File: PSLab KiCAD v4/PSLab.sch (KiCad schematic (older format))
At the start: 69 parts, among them CON1 USB-MICRO-B, J1 Programmer, J12 Sensors, J2 SQRs, J3 LA, J4 OSC_Pins, J6 I2C, J7 IDs, J8 TX_RX_ES, J9 Test_Vs, P7 NRF, Q2 MMBT3904, Q3 MMBT3906, U1 MCP2200, U15 ESP8266, U2 74HC126, U3 PIC24EP256GP204, U4 TC1240A, U5 7660, U6 LM1117-3.3, X1 12MHz

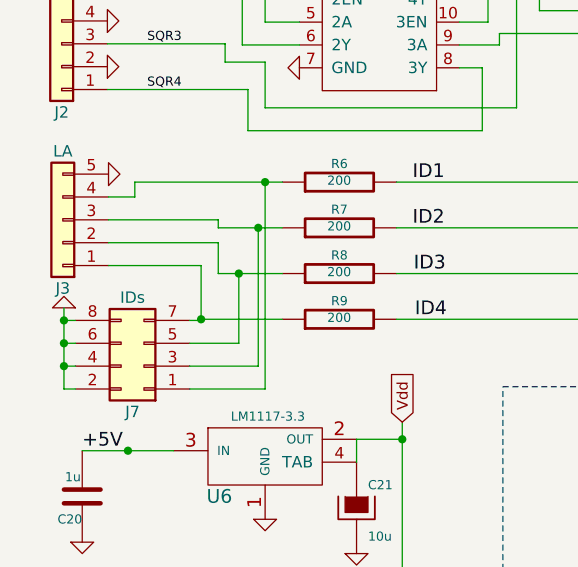
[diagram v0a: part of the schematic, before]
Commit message: Optimizing layout
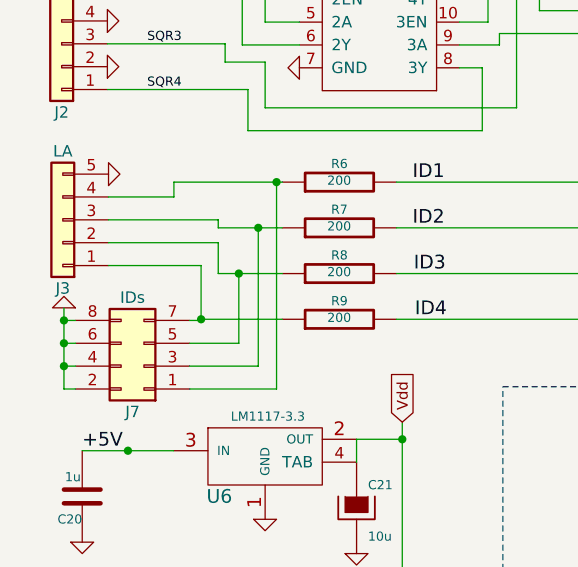
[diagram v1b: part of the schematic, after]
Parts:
- C1, C10, C13, C17, C2, C4, C5, C8, C9: footprint Capacitors_SMD:C_0201 -> Capacitors_SMD:C_0603
- C15, C20, C21: footprint Capacitors_SMD:C_0402 -> Capacitors_SMD:C_0603
- R1, R10, R11, R12, R13, R2, R3, R4, R49, R5, R52, R53, R54, R55, R56, R57, R6, R7, R8, R9: footprint Resistors_SMD:R_0201 -> Resistors_SMD:R_0603

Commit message: Programmer pin header adjustments
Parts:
- P7: footprint Custom_Components:nRF24L01_Breakout_2 -> Pin_Headers:Pin_Header_Straight_2x04_Pitch2.54mm
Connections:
- net GND: now also J1.4 (Pin_4); no longer J1.2 (Pin_2)
- net MCLR: now also J1.2 (Pin_2); no longer J1.6 (Pin_6)
- net PGC2: now also J1.6 (Pin_6); no longer J1.5 (Pin_5)
- net PGD2: now also J1.5 (Pin_5); no longer J1.4 (Pin_4)
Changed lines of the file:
@@
 F 0 "P7" H 1505 7675 50  0000 C CNN
 F 1 "NRF" H 1505 7175 50  0000 C CNN
-F 2 "Custom_Components:nRF24L01_Breakout_2" H 1505 6225 60  0001 C CNN
+F 2 "Pin_Headers:Pin_Header_Straight_2x04_Pitch2.54mm" H 1505 6225 60  0001 C CNN
 F 3 "" H 1505 6225 60  0000 C CNN
 	1    1505 7425
@@
 Text GLabel 5020 1020 2    40   Input ~ 0
 PGD2
-Text GLabel 4670 7005 0    40   Input ~ 0
+Text GLabel 4670 7105 0    40   Input ~ 0
 PGD2
-Text GLabel 4670 7105 0    40   Input ~ 0
+Text GLabel 4670 7205 0    40   Input ~ 0
 PGC2
 $Comp
@@
 L GND-RESCUE-proto1 #PWR048
 U 1 1 5A56D115
-P 4670 6805
-F 0 "#PWR048" H 4670 6805 30  0001 C CNN
-F 1 "GND" H 4670 6735 30  0001 C CNN
-F 2 "" H 4670 6805 60  0000 C CNN
-F 3 "" H 4670 6805 60  0000 C CNN
-	1    4670 6805
-	0    1    1    0
-$EndComp
-Text GLabel 4670 7205 0    40   Input ~ 0
+P 4670 7005
+F 0 "#PWR048" H 4670 7005 30  0001 C CNN
+F 1 "GND" H 4670 6935 30  0001 C CNN
+F 2 "" H 4670 7005 60  0000 C CNN
+F 3 "" H 4670 7005 60  0000 C CNN
+	1    4670 7005
+	0    1    1    0
+$EndComp
+Text GLabel 4670 6805 0    40   Input ~ 0
 MCLR
 Text GLabel 4545 815  0    40   Input ~ 0

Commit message: Added Gerber files
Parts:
- added TP3, TP4: TEST, Measurement_Points:Measurement_Point_Round-SMD-Pad_Small, symbol TEST
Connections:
- net +5V: now also TP3.1
- net GND: now also TP4.1
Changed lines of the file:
@@
 	1550 5355 1550 4450
 Connection ~ 1550 4450
+$Comp
+L TEST TP3
+U 1 1 5A66A817
+P 850 1930
+F 0 "TP3" H 850 2230 50  0000 C BNN
+F 1 "TEST" H 850 2180 50  0000 C CNN
+F 2 "Measurement_Points:Measurement_Point_Round-SMD-Pad_Small" H 850 1930 50  0001 C CNN
+F 3 "" H 850 1930 50  0001 C CNN
+	1    850  1930
+	1    0    0    -1
+$EndComp
+$Comp
+L TEST TP4
+U 1 1 5A66B7F8
+P 2285 1925
+F 0 "TP4" H 2285 2225 50  0000 C BNN
+F 1 "TEST" H 2285 2175 50  0000 C CNN
+F 2 "Measurement_Points:Measurement_Point_Round-SMD-Pad_Small" H 2285 1925 50  0001 C CNN
+F 3 "" H 2285 1925 50  0001 C CNN
+	1    2285 1925
+	1    0    0    -1
+$EndComp
+$Comp
+L GND-RESCUE-proto1 #PWR056
+U 1 1 5A66B8E0
+P 2285 1925
+F 0 "#PWR056" H 2285 1925 30  0001 C CNN
+F 1 "GND" H 2285 1855 30  0001 C CNN
+F 2 "" H 2285 1925 60  0000 C CNN
+F 3 "" H 2285 1925 60  0000 C CNN
+	1    2285 1925
+	1    0    0    -1
+$EndComp
 $EndSCHEMATC

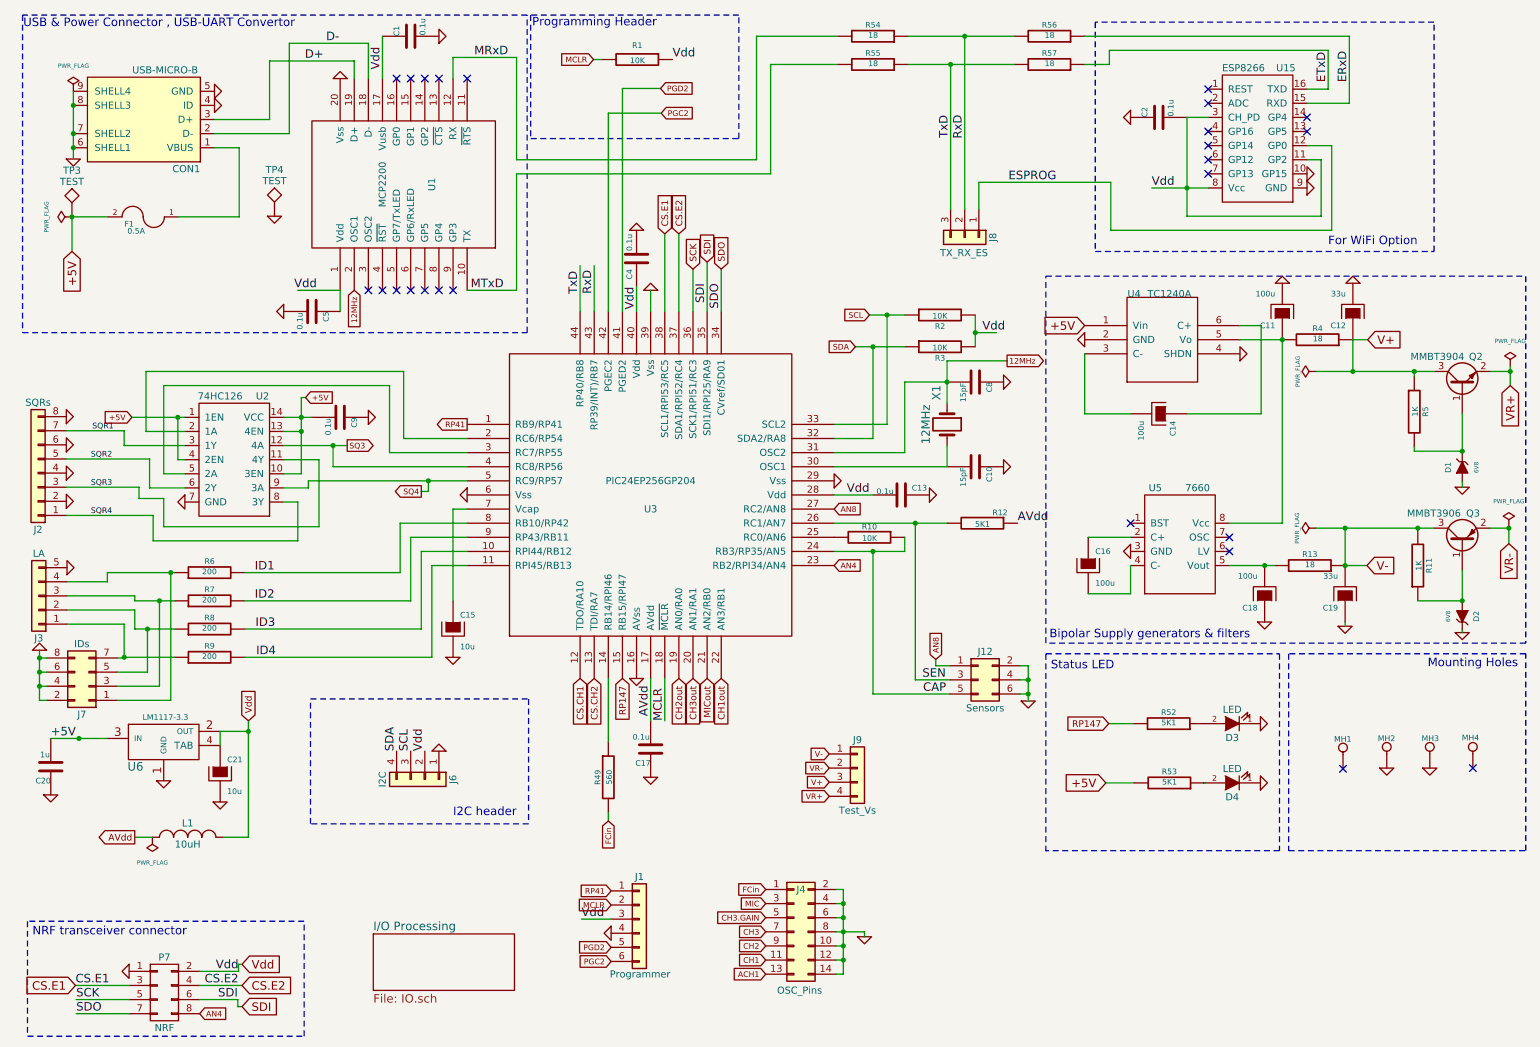
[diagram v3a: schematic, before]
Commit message: Added breakouts for MCP2200 & PIC24 (#36)
* Added breakouts for MCP2200

* Added guard rings for OSC

* Grounded mount holes

* Gerber files updated
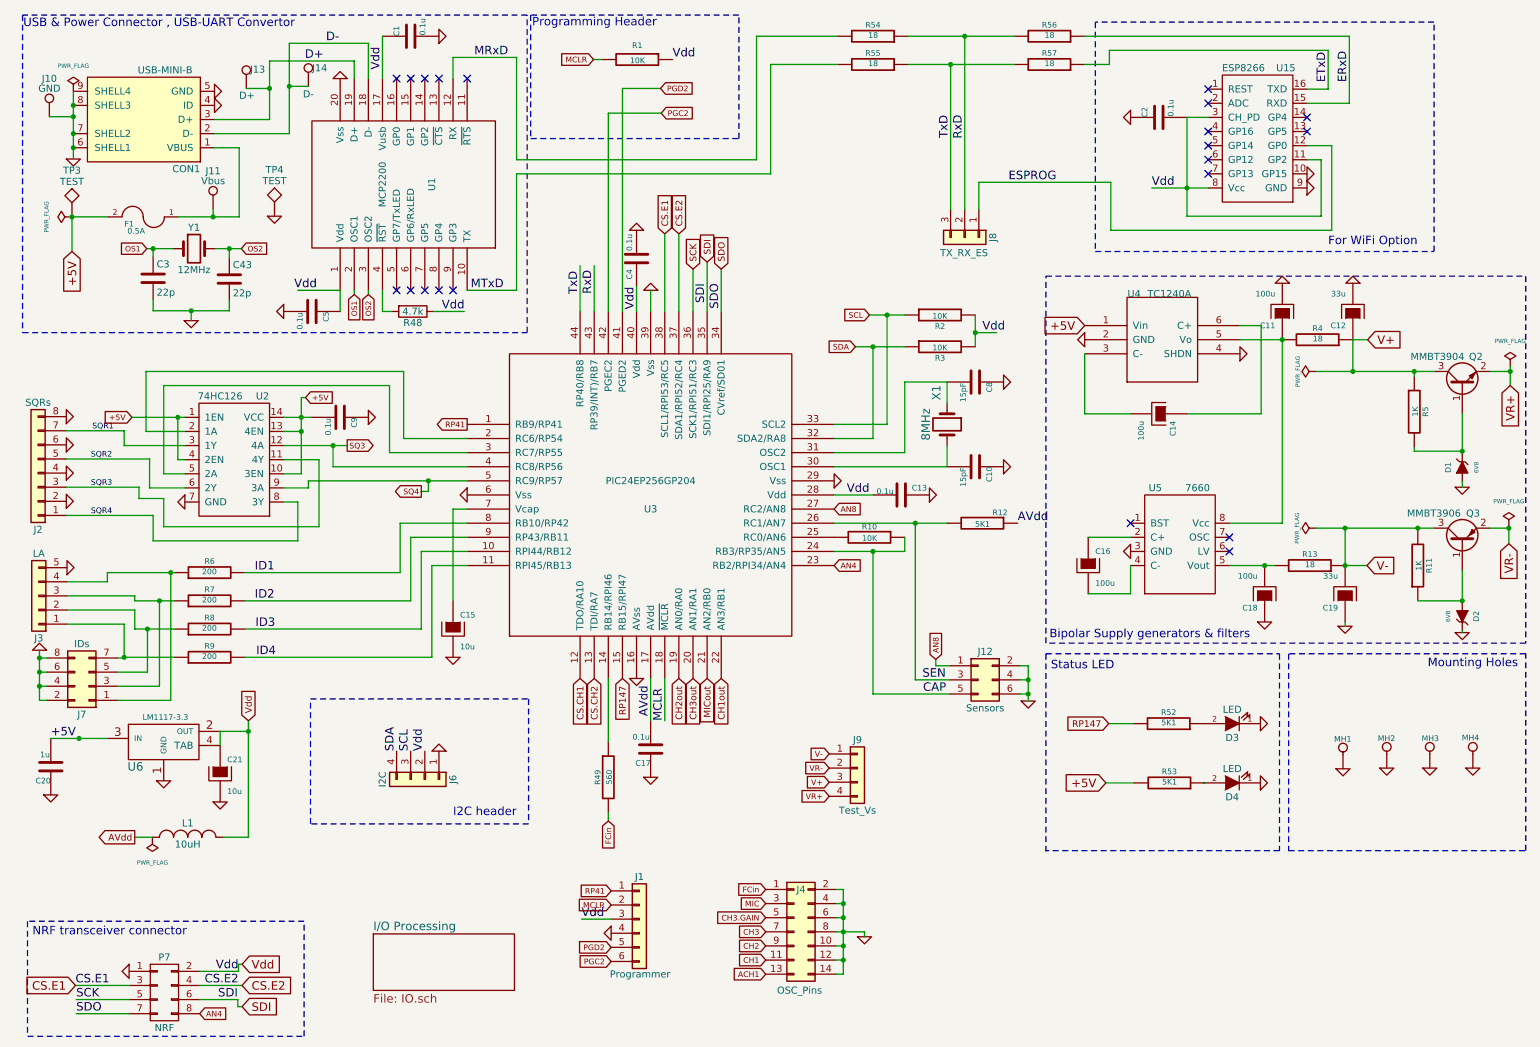
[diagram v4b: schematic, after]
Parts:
- added C3, C43: 22p, Capacitors_SMD:C_0603, symbol C
- added J10: GND, Measurement_Points:Measurement_Point_Square-SMD-Pad_Small, symbol TEST_1P
- added J11: Vbus, Measurement_Points:Measurement_Point_Square-SMD-Pad_Small, symbol TEST_1P
- added J13: D+, Measurement_Points:Measurement_Point_Square-SMD-Pad_Small, symbol TEST_1P
- added J14: D-, Measurement_Points:Measurement_Point_Square-SMD-Pad_Small, symbol TEST_1P
- added R48: 4.7k, Resistors_SMD:R_0603, symbol R
- added Y1: 12MHz, Crystals:Crystal_SMD_5032-2pin_5.0x3.2mm, symbol Crystal
- CON1: value USB-MICRO-B -> USB-MINI-B
- D3, D4: footprint LEDs:LED_0805 -> LEDs:LED_0603
- L1: footprint Inductors_SMD:L_0805 -> Inductors_SMD:L_0603
- X1: value 12MHz -> 8MHz; footprint Crystals:Crystal_HC49-U_Vertical -> Crystals:Crystal_SMD_5032-2pin_5.0x3.2mm
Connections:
- net D+: now also J13.1
- net D-: now also J14.1
- net GND: now also MH1.1, MH4.1, C3.2, C43.2, J10.1
- net Vdd: now also R48.1
- net OS2: now reaches U1.3 (OSC2)
- net OS2: now also C43.1, Y1.2
- net at U1.4 (~RST): now also R48.2
- net at CON1.1 (VBUS), F1.1: now also J11.1
- net 12MHz: no longer names the net of C8.2, U3.31 (OSC2), X1.1
- net 12MHz: no longer U1.2 (OSC1)
- new net OS1: C3.1, U1.2 (OSC1), Y1.1
- no-connect marks 25 -> 21
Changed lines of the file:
@@
 NoConn ~ 3450 2450
 NoConn ~ 3350 2450
-NoConn ~ 3050 2450
 $Comp
 L CONN_1 MH1
@@
 P 7050 3400
 F 0 "X1" H 6825 3325 60  0000 C CNN
-F 1 "12MHz" H 7050 3250 60  0000 C CNN
-F 2 "Crystals:Crystal_HC49-U_Vertical" H 7050 3400 60  0001 C CNN
+F 1 "8MHz" H 7050 3250 60  0000 C CNN
+F 2 "Crystals:Crystal_SMD_5032-2pin_5.0x3.2mm" H 7050 3400 60  0001 C CNN
 F 3 "" H 7050 3400 60  0000 C CNN
 	1    7050 3400
@@
 F 0 "L1" H 1670 6425 50  0000 C CNN
 F 1 "10uH" H 1670 6275 50  0000 C CNN
-F 2 "Inductors_SMD:L_0805" H 1670 6325 60  0001 C CNN
+F 2 "Inductors_SMD:L_0603" H 1670 6325 60  0001 C CNN
 F 3 "" H 1670 6325 60  0000 C CNN
 	1    1670 6325
@@
 Text GLabel 3325 3875 0    40   Output ~ 0
 SQ4
-NoConn ~ 2950 2450
 $Comp
 L GND-RESCUE-proto1 #PWR041
@@
 Text GLabel 1755 7575 2    40   Input ~ 0
 AN4
-Text GLabel 7475 2950 2    40   Output ~ 0
-12MHz
-Text GLabel 2850 2450 3    40   Input ~ 0
-12MHz
 Text GLabel 2800 3550 2    40   Output ~ 0
 SQ3
@@
 F 0 "D3" H 9070 5620 50  0000 C CNN
 F 1 "LED" H 9070 5420 50  0000 C CNN
-F 2 "LEDs:LED_0805" H 9070 5520 60  0001 C CNN
+F 2 "LEDs:LED_0603" H 9070 5520 60  0001 C CNN
 F 3 "" H 9070 5520 60  0000 C CNN
 	1    9070 5520
@@
 F 0 "D4" H 9070 6040 50  0000 C CNN
 F 1 "LED" H 9070 5840 50  0000 C CNN
-F 2 "LEDs:LED_0805" H 9070 5940 60  0001 C CNN
+F 2 "LEDs:LED_0603" H 9070 5940 60  0001 C CNN
 F 3 "" H 9070 5940 60  0000 C CNN
 	1    9070 5940
@@
 $EndComp
 $Comp
-L USB-MINI-B CON1
-U 1 1 556D8B03
-P 1360 1240
-F 0 "CON1" H 1060 1590 50  0000 C CNN
-F 1 "USB-MICRO-B" H 1210 890 50  0000 C CNN
-F 2 "Connectors:USB_Micro-B" H 1360 1140 50  0001 C CNN
-F 3 "" H 1360 1140 50  0000 C CNN
-	1    1360 1240
-	-1   0    0    1
-$EndComp
-$Comp
 L Conn_01x03 J8
 U 1 1 5A320F8A
@@
 	0    -1   -1   0
 $EndComp
-NoConn ~ 9855 5840
-NoConn ~ 10775 5835
 $Comp
 L Conn_02x03_Odd_Even J12
@@
 	2030 7275 1755 7275
 Wire Wire Line
-	860  1040 860  1520
-Connection ~ 860  1440
-Wire Wire Line
 	1375 3450 1650 3450
 Wire Wire Line
@@
 Wire Wire Line
 	1420 6325 1295 6325
-Wire Wire Line
-	7050 2950 7050 3250
-Wire Wire Line
-	7050 2950 7475 2950
 Connection ~ 2700 3550
 Wire Wire Line
@@
 Wire Wire Line
 	7050 3700 7050 3550
-Connection ~ 7050 3100
 Wire Wire Line
 	2030 7225 2030 7275
@@
 	2390 1340 1860 1340
 Wire Wire Line
-	865  1340 860  1340
-Connection ~ 860  1340
+	860  1340 865  1340
 Wire Wire Line
 	865  1140 860  1140
-Connection ~ 860  1140
 Wire Wire Line
 	1605 1930 2035 1930
@@
 	1    0    0    -1
 $EndComp
+$Comp
+L USB-MINI-B CON1
+U 1 1 5A6CB48C
+P 1360 1240
+F 0 "CON1" H 1060 1590 50  0000 C CNN
+F 1 "USB-MINI-B" H 1210 890 50  0000 C CNN
+F 2 "Connectors:USB_Micro-B" H 1360 1140 50  0001 C CNN
+F 3 "" H 1360 1140 50  0000 C CNN
+	1    1360 1240
+	-1   0    0    1
+$EndComp
+Wire Wire Line
+	860  1040 860  1520
+Connection ~ 860  1440
+Connection ~ 860  1340
+Connection ~ 860  1140
+$Comp
+L R R48
+U 1 1 5A6CD97F
+P 3265 2600
+F 0 "R48" V 3345 2600 50  0000 C CNN
+F 1 "4.7k" V 3265 2600 50  0000 C CNN
+F 2 "Resistors_SMD:R_0603" V 3195 2600 50  0001 C CNN
+F 3 "" H 3265 2600 50  0001 C CNN
+	1    3265 2600
+	0    1    1    0
+$EndComp
+Wire Wire Line
+	3050 2450 3050 2600
+Wire Wire Line
+	3050 2600 3115 2600
+Text Label 3470 2600 0    60   ~ 0
+Vdd
+Wire Wire Line
+	3415 2600 3630 2600
+$Comp
+L Crystal Y1
+U 1 1 5A6D25F9
+P 1715 2155
+F 0 "Y1" H 1715 2305 50  0000 C CNN
+F 1 "12MHz" H 1715 2005 50  0000 C CNN
+F 2 "Crystals:Crystal_SMD_5032-2pin_5.0x3.2mm" H 1715 2155 50  0001 C CNN
+F 3 "" H 1715 2155 50  0001 C CNN
+	1    1715 2155
+	1    0    0    -1
+$EndComp
+$Comp
+L C C3
+U 1 1 5A6D2A55
+P 1425 2365
+F 0 "C3" H 1450 2465 50  0000 L CNN
+F 1 "22p" H 1450 2265 50  0000 L CNN
+F 2 "Capacitors_SMD:C_0603" H 1463 2215 50  0001 C CNN
+F 3 "" H 1425 2365 50  0001 C CNN
+	1    1425 2365
+	1    0    0    -1
+$EndComp
+$Comp
+L C C43
+U 1 1 5A6D2B78
+P 1965 2370
+F 0 "C43" H 1990 2470 50  0000 L CNN
+F 1 "22p" H 1990 2270 50  0000 L CNN
+F 2 "Capacitors_SMD:C_0603" H 2003 2220 50  0001 C CNN
+F 3 "" H 1965 2370 50  0001 C CNN
+	1    1965 2370
+	1    0    0    -1
+$EndComp
+Wire Wire Line
+	1865 2155 2050 2155
+Wire Wire Line
+	1965 2155 1965 2220
+$Comp
+L GND-RESCUE-proto1 #PWR057
+U 1 1 5A6D3C13
+P 1695 2665
+F 0 "#PWR057" H 1695 2665 30  0001 C CNN
+F 1 "GND" H 1695 2595 30  0001 C CNN
+F 2 "" H 1695 2665 60  0000 C CNN
+F 3 "" H 1695 2665 60  0000 C CNN
+	1    1695 2665
+	1    0    0    -1
+$EndComp
+Wire Wire Line
+	1380 2155 1565 2155
+Wire Wire Line
+	1425 2155 1425 2215
+Wire Wire Line
+	1425 2515 1425 2595
+Wire Wire Line
+	1425 2595 1965 2595
+Wire Wire Line
+	1965 2595 1965 2520
+Wire Wire Line
+	1695 2665 1695 2595
+Connection ~ 1695 2595
+Text GLabel 1380 2155 0    39   Input ~ 0
+OS1
+Text GLabel 2050 2155 2    39   Input ~ 0
+OS2
+Connection ~ 1965 2155
+Connection ~ 1425 2155
+Text GLabel 2850 2480 3    39   Input ~ 0
+OS1
+Wire Wire Line
+	2850 2480 2850 2450
+Text GLabel 2950 2480 3    39   Input ~ 0
+OS2
+Wire Wire Line
+	2950 2480 2950 2450
+Wire Wire Line
+	7050 3250 7050 3100
+$Comp
+L TEST_1P J13
+U 1 1 5A6F40E4
+P 2085 1020
+F 0 "J13" H 2165 1155 50  0000 C CNN
+F 1 "D+" H 2090 970 50  0000 C CNN
+F 2 "Measurement_Points:Measurement_Point_Square-SMD-Pad_Small" H 2285 1020 50  0001 C CNN
+F 3 "" H 2285 1020 50  0001 C CNN
+	1    2085 1020
+	1    0    0    -1
+$EndComp
+$Comp
+L TEST_1P J14
+U 1 1 5A6F42FD
+P 2525 1005
+F 0 "J14" H 2605 1135 50  0000 C CNN
+F 1 "D-" H 2525 950 50  0000 C CNN
+F 2 "Measurement_Points:Measurement_Point_Square-SMD-Pad_Small" H 2725 1005 50  0001 C CNN
+F 3 "" H 2725 1005 50  0001 C CNN
+	1    2525 1005
+	1    0    0    -1
+$EndComp
+Wire Wire Line
+	2525 1005 2390 1005
+Connection ~ 2390 1005
+Wire Wire Line
+	2085 1020 2250 1020
+Connection ~ 2250 1020
+$Comp
+L TEST_1P J11
+U 1 1 5A6F5463
+P 1850 1875
+F 0 "J11" H 1850 2145 50  0000 C CNN
+F 1 "Vbus" H 1850 2075 50  0000 C CNN
+F 2 "Measurement_Points:Measurement_Point_Square-SMD-Pad_Small" H 2050 1875 50  0001 C CNN
+F 3 "" H 2050 1875 50  0001 C CNN
+	1    1850 1875
+	1    0    0    -1
+$EndComp
+$Comp
+L TEST_1P J10
+U 1 1 5A6F58A7
+P 690 1220
+F 0 "J10" H 690 1490 50  0000 C CNN
+F 1 "GND" H 690 1420 50  0000 C CNN
+F 2 "Measurement_Points:Measurement_Point_Square-SMD-Pad_Small" H 890 1220 50  0001 C CNN
+F 3 "" H 890 1220 50  0001 C CNN
+	1    690  1220
+	1    0    0    -1
+$EndComp
+Wire Wire Line
+	690  1220 860  1220
+Connection ~ 860  1220
+Wire Wire Line
+	1850 1875 1850 1930
+Connection ~ 1850 1930
+$Comp
+L GND-RESCUE-proto1 #PWR058
+U 1 1 5A6F58C4
+P 10775 5835
+F 0 "#PWR058" H 10775 5835 30  0001 C CNN
+F 1 "GND" H 10775 5765 30  0001 C CNN
+F 2 "" H 10775 5835 60  0000 C CNN
+F 3 "" H 10775 5835 60  0000 C CNN
+	1    10775 5835
+	1    0    0    -1
+$EndComp
+$Comp
+L GND-RESCUE-proto1 #PWR059
+U 1 1 5A6F5AA9
+P 9855 5840
+F 0 "#PWR059" H 9855 5840 30  0001 C CNN
+F 1 "GND" H 9855 5770 30  0001 C CNN
+F 2 "" H 9855 5840 60  0000 C CNN
+F 3 "" H 9855 5840 60  0000 C CNN
+	1    9855 5840
+	1    0    0    -1
+$EndComp

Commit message: Updated docs with new layout
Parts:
- C10, C8: value 15pF -> 33pF
- C3, C43: value 22p -> 33p
- D3, D4: footprint LEDs:LED_0603 -> LEDs:LED_0805
- R48: value 4.7k -> 5k1
- R49: value 560 -> 200
- U3: symbol PIC24EP64GP204 -> PIC24EP256GP204
- X1: value 8MHz -> 12MHz
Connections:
- net AVdd: now also L1.2; no longer L1.1
- net Vdd: now also L1.1; no longer L1.2
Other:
- note added: "Bipolar Supply Generators & Filters"
- note added: "Expansions"
- note added: "I/O Processing"
- note added: "NRF Transceiver Connector"
- note added: "Regulator"
- note removed: "Bipolar Supply generators & filters"
- note removed: "I2C header\n"
- note removed: "NRF transceiver connector\n"
- moved on the sheet: C20, C21, J1, J3, J4, J6, J7, J9, L1, P7, R6, R7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
